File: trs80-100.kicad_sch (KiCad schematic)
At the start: 339 parts, among them CN2 A-7224, CN3 TCS-4480, CN4 TCS-4490, CN5 PRINTER CONNECTOR, CN6 RS232C, CN7 LCD-CONN, CN8 LCD-LED-CONN, J1 Adapter Jack CN9, K1 Key_Board, M1 40H373, M10 SystemBus, M11 ROM32k, M12 ROM32k, M13 40H032, M14 40H175, M15 40H244, M16 40H138, M17 40H000, M18 μPD1990AC, M19 80C85, M2 40H245, M20 40H367, M21 40H244, M22 IM6402, M23 40H244, M24 40H032, M25 81C55, M26 40H002, M27 4011, M28 4013, M29 TL064, M3 40H138, M30 TL064, M31 MC14412, M32 40H244, M33 40H157, M34 4584, M35 4584, M4 40H138, M5 40H139, M6 OPTION RAM #3, M7 OPTION RAM #2, M8 OPTION RAM #1, M9 STANDARD RAM, SW3 SLB-22BP-03, SW4 Reset Switch, SW5 SSP32201, T1 2SA1115, T10 2SC2603, T11 2SC2603, T13 2SC2603, T14 2SC2603(E), T15 2SC2603(E), T16 2SC2603(E), T17 2SC2603(E), T18 2SC2603, T19 2SA1115, T2 2SC2603, T20 2SC2603, T21 2SC2603(E), T22 2SC2603(E), T25 2SC2603, T27 2SC2603, T28 2SA1115, T3 2SC2603, T5 2SC2603, T6 2SC2603, T8 2SC2603, T9 2SC2603, X1 32.768kHz, X2 4.9152MHz, X3 1.0MHz

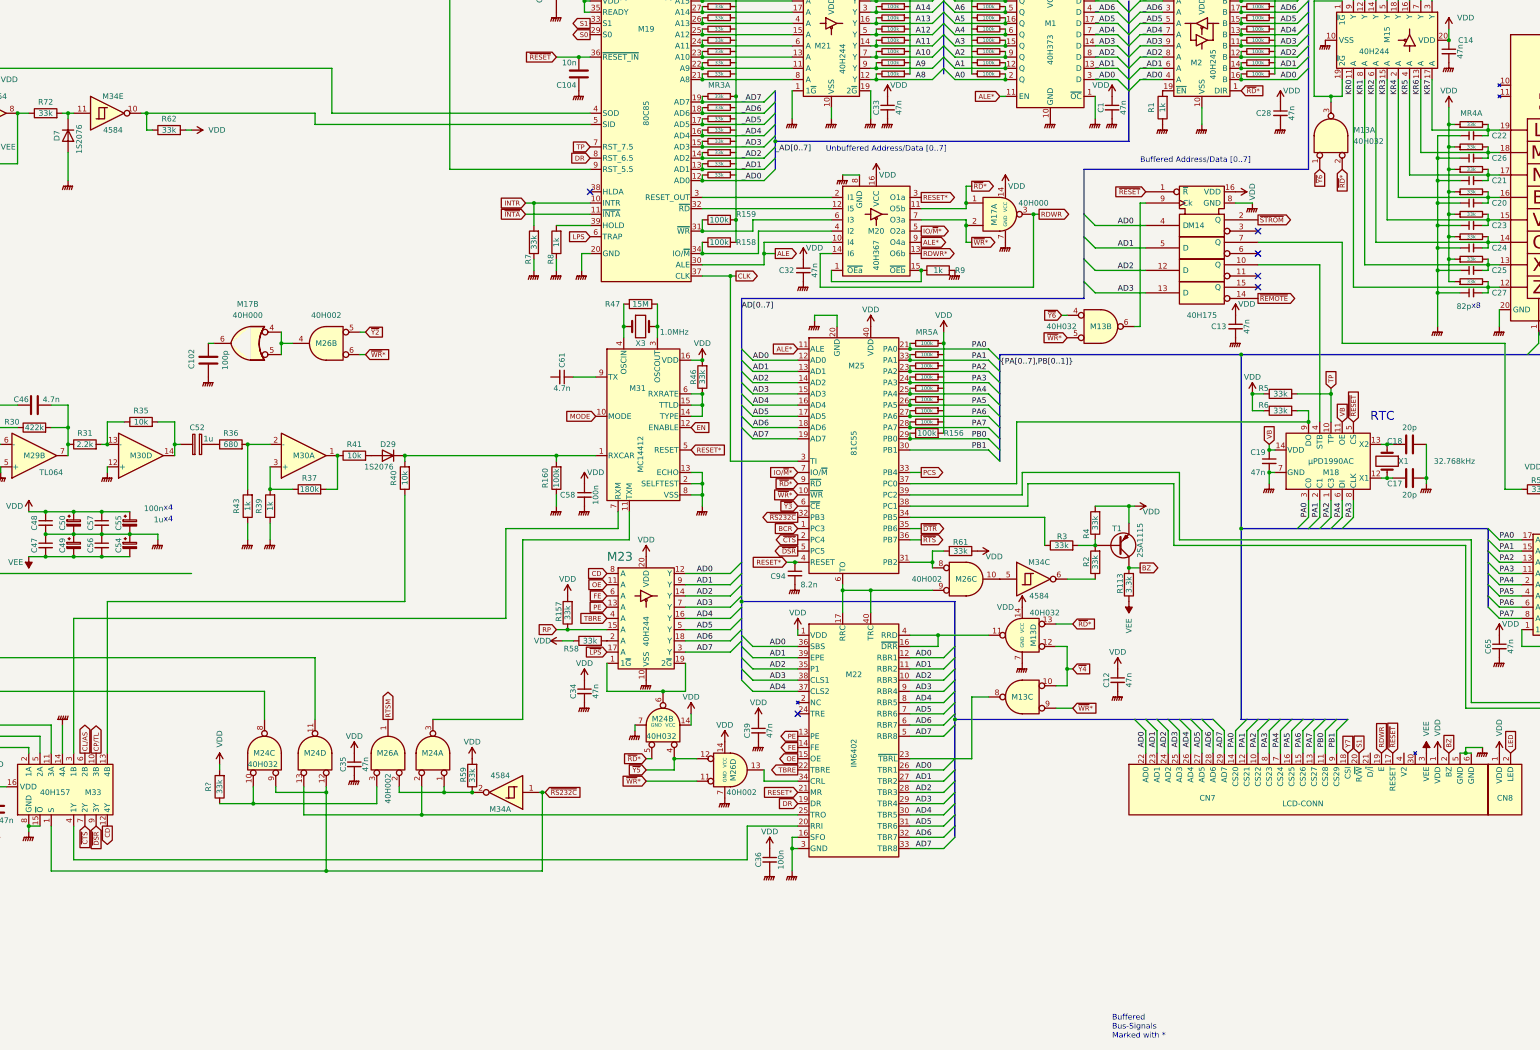
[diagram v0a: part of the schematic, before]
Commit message: Add LCD contrast circuit.
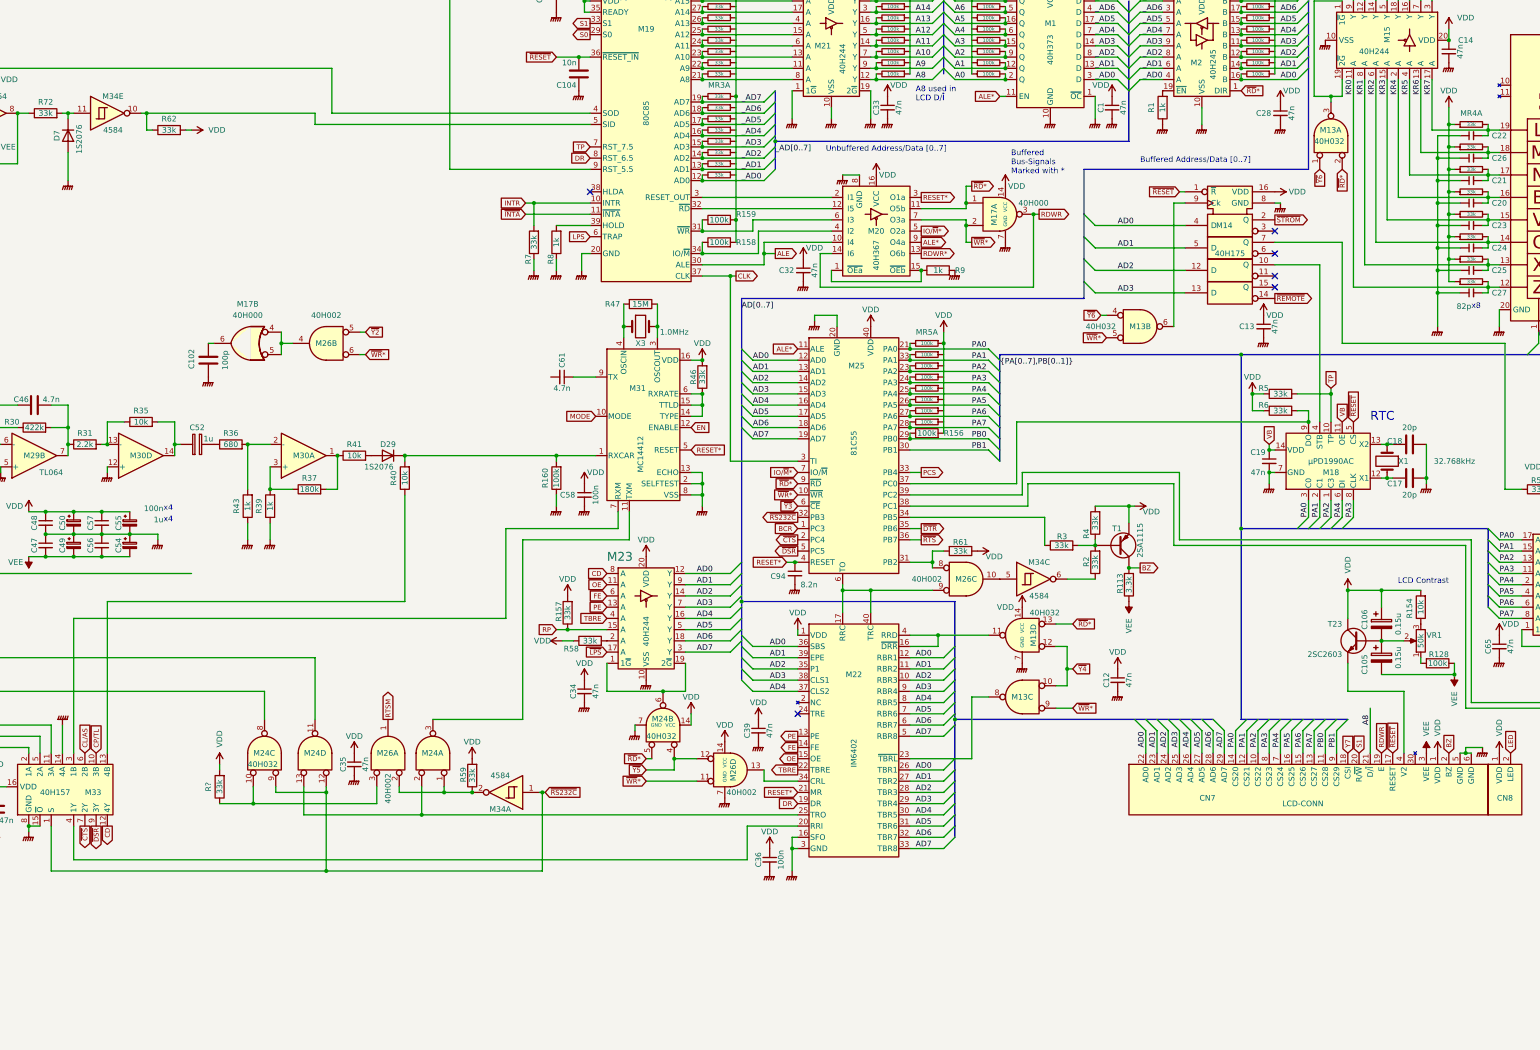
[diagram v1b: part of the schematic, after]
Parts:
- added C105, C106: 0.15u, symbol Device:C_Polarized
- added R128: 100k, symbol Device:R
- added R154: 10k, symbol Device:R
- added T23: 2SC2603, Package_TO_SOT_THT:TO-92_Inline, symbol Transistor_BJT:2N3904
- added VR1: 50k, symbol Device:R_Potentiometer
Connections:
- net A8: now also CN7.21 (D/~{I})
- net VDD: now also C106.1, R154.2, T23.3 (C)
- net VEE: now also C105.2, R128.1
- net at CN7.4 (V2): now also T23.1 (E)
- new net: C105.1, C106.2, T23.2 (B), VR1.2
- new net: R154.1, VR1.3
- new net: R128.2, VR1.1
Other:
- note added: "A8 used in LCD D/~{I}"
- note added: "LCD Contrast"
- moved on the sheet: C13, M13B, M14

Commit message: Add first modem relay.
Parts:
- added C91: 47n, symbol Device:C_Small
- added D21: 1S2076, symbol Device:D
- added M36: 4013, symbol 4xxx:4013
- added R134: 3.3k, symbol Device:R
- added R136: 68k, symbol Device:R
- added R146: 33k, symbol Device:R
- added RY3: FRL-764D05/1BS-T, symbol trs80-100:FRL-764D05/1BS-T
- added T24: 2SC2603, Package_TO_SOT_THT:TO-92_Inline, symbol Transistor_BJT:2N3904
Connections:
- net AD0: now also M36.5 (D)
- net AD1: now also M36.9 (D)
- net EN: now also M36.13 (Q), R146.1
- net GNDPWR: now also R93.1, C91.2, M36.6 (S), M36.7 (VSS), M36.8 (S), R136.2, T24.1 (E); no longer R93.2
- net RESET*: now also M36.10 (R), M36.4 (R)
- net VDD: now also C91.1, M36.14 (VDD), R146.2
- net VR: now also D21.1 (K), RY3.4
- net at C102.2, M17.6: now also M36.11 (C), M36.3 (C)
- net at R50.1, T6.2 (B): now also R93.2; no longer R93.1
- net at CN4.1 (TL): now also RY3.2
- new net: R134.2, R136.1, T24.2 (B)
- new net: D21.2 (A), RY3.3, T24.3 (C)
- new net: M36.1 (Q), R134.1
- no-connect marks 19 -> 21
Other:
- note added: "Cassette Remote Control"
- note added: "Periphery select IO=1 ADDR: 0x8xxx-0xFxxx"
- note removed: "Periphery address"
- moved on the sheet: C102, C13, C15, M17B, M26B, M34B, R50, R67, R93, T6

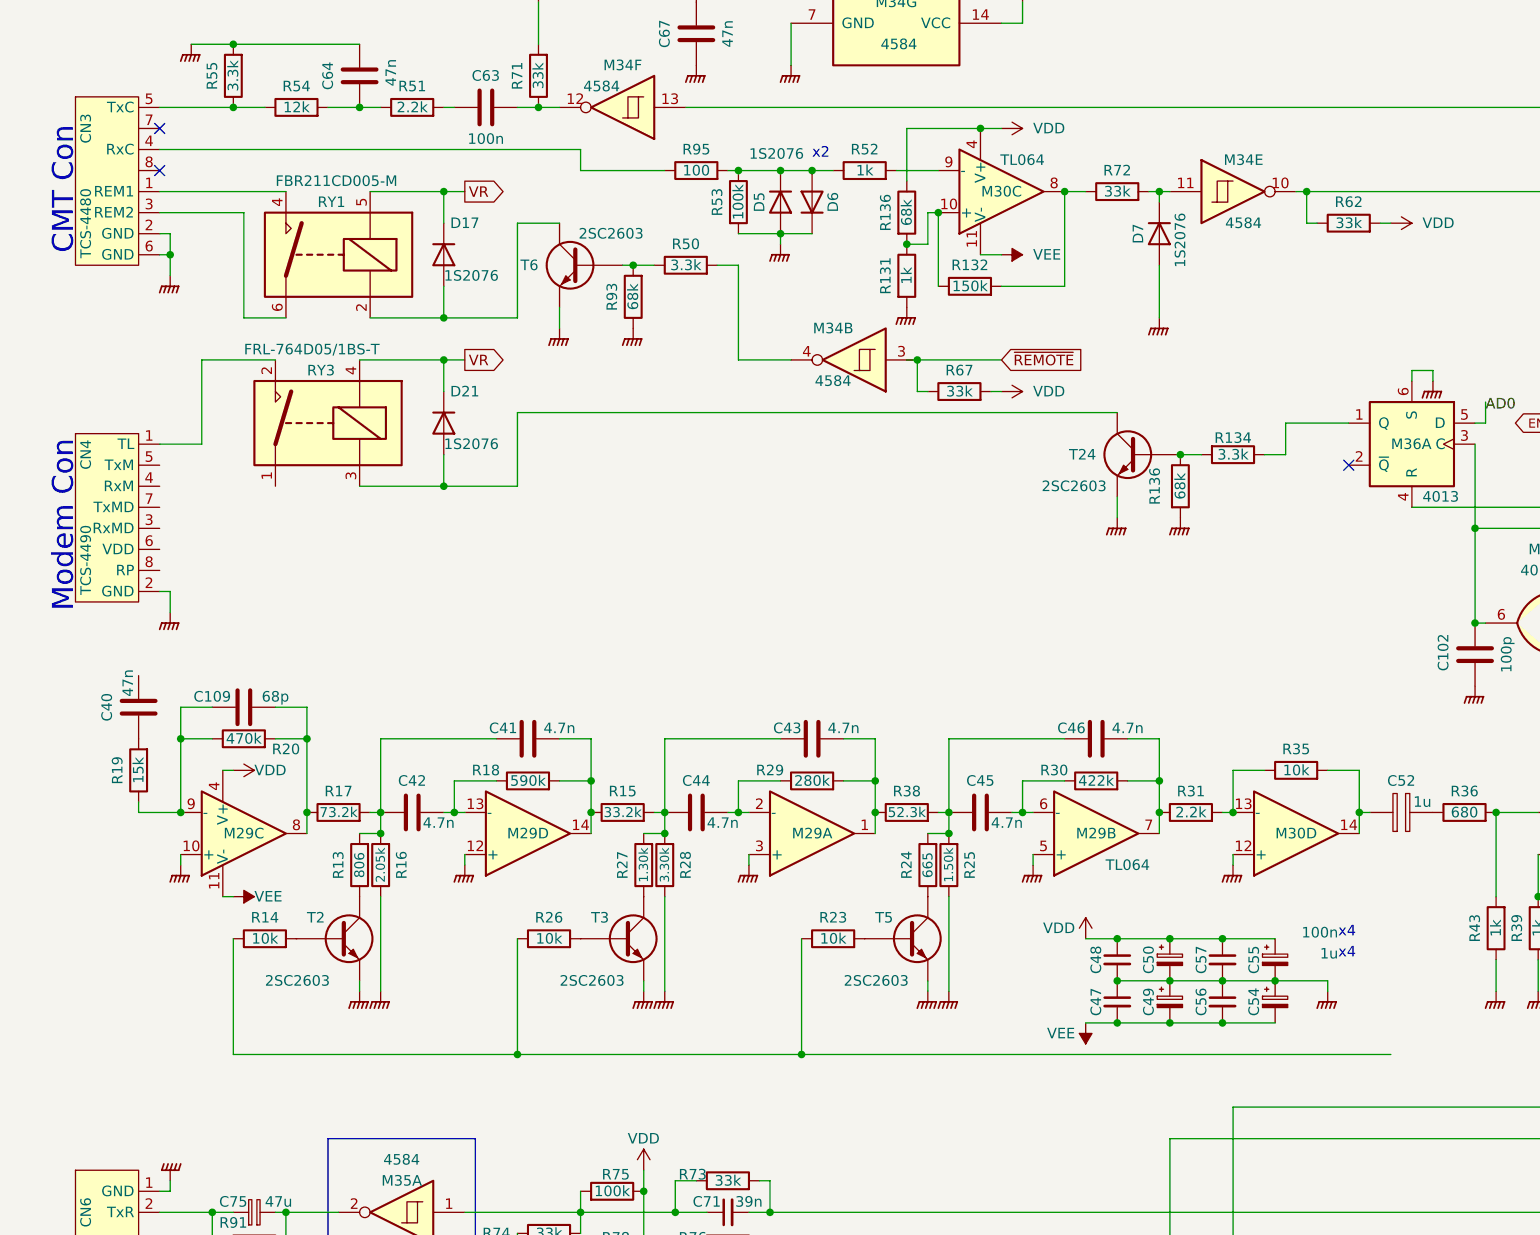
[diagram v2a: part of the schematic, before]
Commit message: Add modem transformer; second relay.
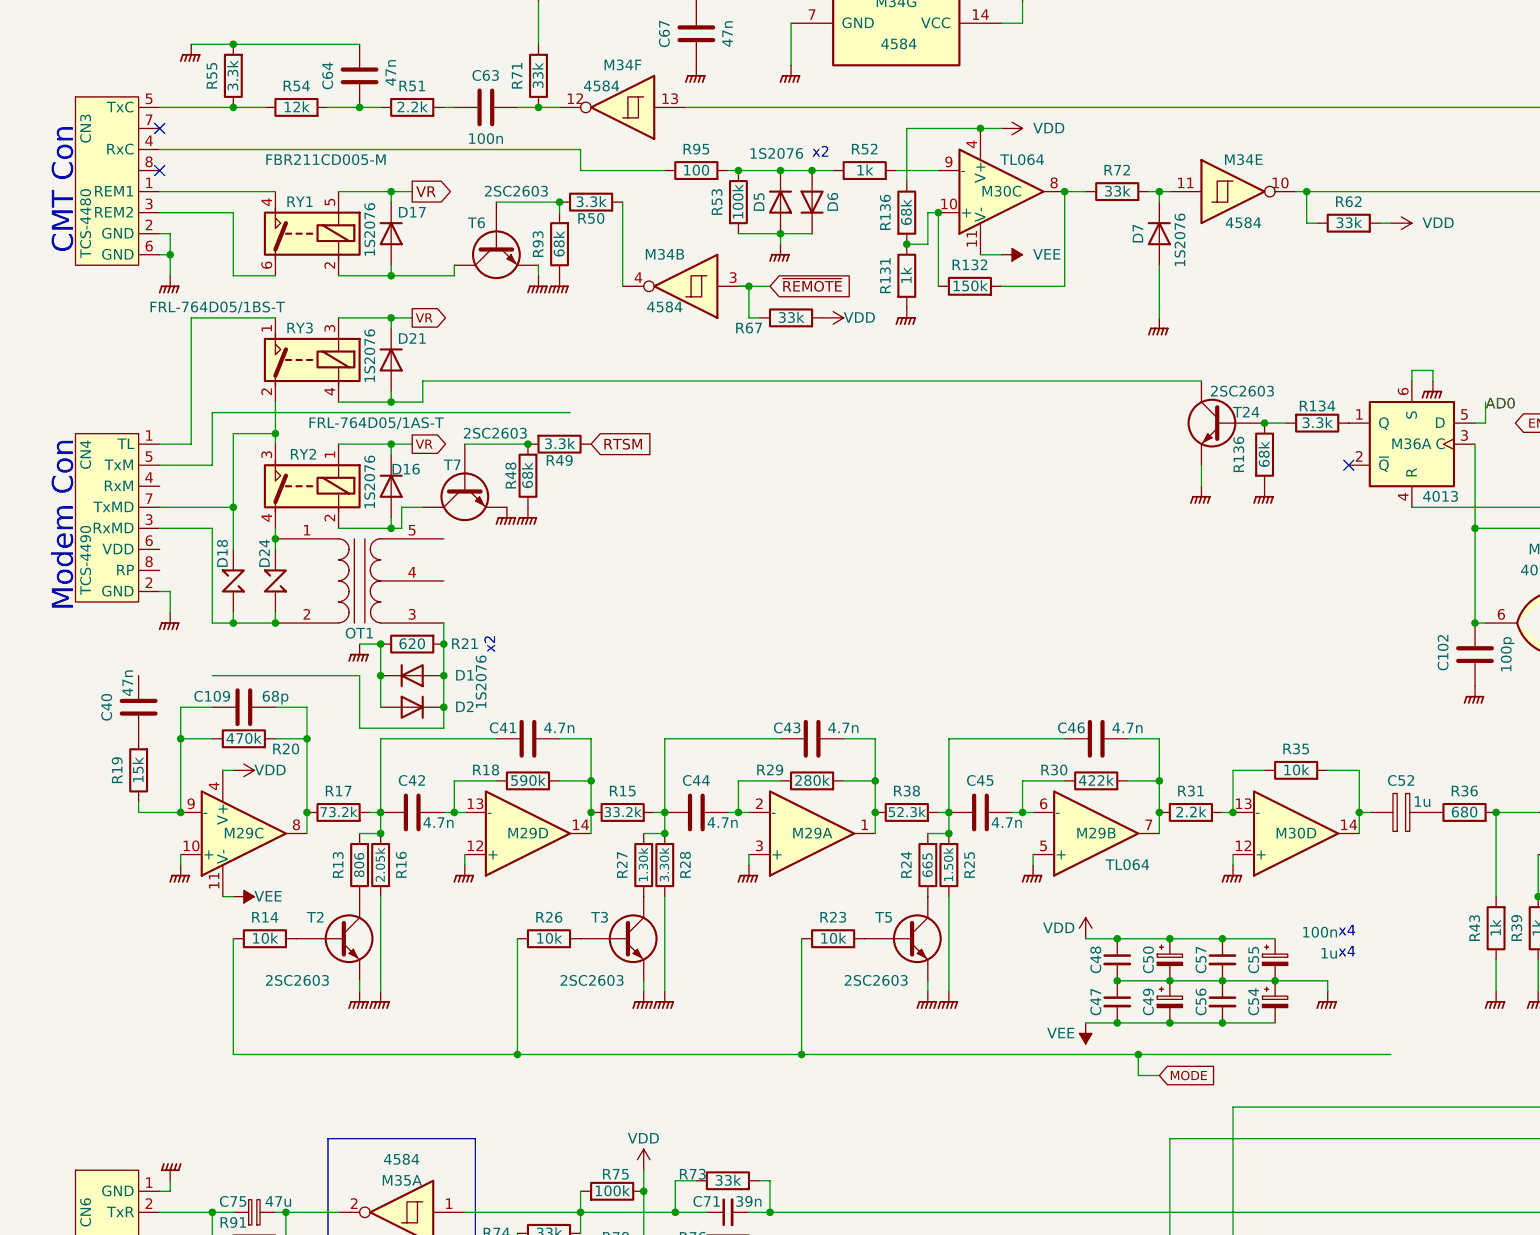
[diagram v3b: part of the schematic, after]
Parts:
- added D1, D16, D2: 1S2076, symbol Device:D
- added D18, D24: surge-absorber, symbol trs80-100:surge-absorber
- added OT1: Transformer_1P_SS, symbol Device:Transformer_1P_SS
- added R21: 620, symbol Device:R
- added R48: 68k, symbol Device:R
- added R49: 3.3k, symbol Device:R
- added RY2: FRL-764D05/1AS-T, symbol trs80-100:FRL-764D05/1AS-T
- added T7: 2SC2603, Package_TO_SOT_THT:TO-92_Inline, symbol Transistor_BJT:2N3904
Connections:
- net GNDPWR: now also D1.1 (K), D2.2 (A), R21.1, R48.1, T7.1 (E)
- net MODE: now also R14.1, R23.1, R26.1
- net RTSM: now also R49.1
- net VR: now also RY3.3, D16.1 (K), RY2.1; no longer RY3.4
- net at RY3.2: now also CN4.7 (TxMD), D18.2 (A), RY2.3; no longer CN4.1 (TL)
- net at CN4.3 (RxMD): now also D18.1 (K), D24.1 (K), OT1.2 (AB)
- net at D21.2 (A), T24.3 (C): now also RY3.4; no longer RY3.3
- net at RY3.1: now also CN4.1 (TL)
- new net: D16.2 (A), RY2.2, T7.3 (C)
- new net: D24.2 (A), OT1.1 (AA), RY2.4
- new net: R48.2, R49.2, T7.2 (B)
- new net: D1.2 (A), D2.1 (K), OT1.3 (SA), R21.2
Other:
- moved on the sheet: D17, D21, M34B, R134, R136, R50, R67, R93, T24, T6
